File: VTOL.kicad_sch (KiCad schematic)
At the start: 36 parts, among them J10 I2C header, J5 USB_C_Receptacle_USB2.0_16P, J6 Conn_01x02_Pin, J7 Pi UART, J8 SEN66, J9 I2C header, SW1 RESET, SW2 BOOT, SW3 SW_SPDT, U4 ESP32-S3-WROOM-1, U5 USBLC6-2SC6, U6 AP7361C-33ER-13, U7 R-78E5.0-1.0

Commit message: new schem
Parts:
- removed C11: 10u 25V, Capacitor_SMD:C_0805_2012Metric_Pad1.18x1.45mm_HandSolder, symbol Device:C
- removed C13: 47u 35V, Capacitor_SMD:CP_Elec_6.3x5.8, symbol Device:C_Polarized
- removed D1: SMF5.0A, Diode_SMD:D_SOD-123F, symbol Diode:PTVS5V0Z1USK
- removed F1: 1A, Fuse:Fuse_1206_3216Metric_Pad1.42x1.75mm_HandSolder, symbol Device:Polyfuse
- removed F2: 0.75A 24V, Fuse:Fuse_1812_4532Metric_Pad1.30x3.40mm_HandSolder, symbol Device:Polyfuse
- removed H5: MountingHole, MountingHole:MountingHole_3.2mm_M3_Pad_Via, symbol Mechanical:MountingHole
- removed J10, J9: I2C header, Connector_PinHeader_2.54mm:PinHeader_1x04_P2.54mm_Vertical, symbol Connector:Conn_01x04_Pin
- removed J5: USB_C_Receptacle_USB2.0_16P, VTOL_parts:USB_C_Receptacle_GCT_USB4105-GF-A_16P_TopMnt_Horizontal_S1, symbol Connector:USB_C_Receptacle_USB2.0_16P
- removed J6: Conn_01x02_Pin, Connector_JST:JST_PH_S2B-PH-K_1x02_P2.00mm_Horizontal, symbol Connector:Conn_01x02_Pin
- removed J7: Pi UART, Connector_PinHeader_2.54mm:PinHeader_1x03_P2.54mm_Vertical, symbol Connector:Conn_01x03_Pin
- removed SW1: RESET, Button_Switch_SMD:SW_SPST_PTS645Sx43SMTR92, symbol Switch:SW_Push
- removed SW2: BOOT, Button_Switch_SMD:SW_SPST_PTS645Sx43SMTR92, symbol Switch:SW_Push
- removed SW3: SW_SPDT, VTOL_parts:SW_Slide_SPDT_RightAngle_CK_1101M2S3AQE2, symbol Switch:SW_SPDT
- removed U4: ESP32-S3-WROOM-1, VTOL_parts:ESP32-S3-WROOM-1_Via0.3mm, symbol RF_Module:ESP32-S3-WROOM-1
- removed U5: USBLC6-2SC6, Package_TO_SOT_SMD:SOT-23-6, symbol Power_Protection:USBLC6-2SC6
- removed U6: AP7361C-33ER-13, Package_TO_SOT_SMD:SOT-223-3_TabPin2, symbol Regulator_Linear:AMS1117-3.3
- removed U7: R-78E5.0-1.0, Converter_DCDC:Converter_DCDC_RECOM_R-78E-0.5_THT, symbol Converter_DCDC:R-78E5.0-1.0
- added C13: 10u 25V, Capacitor_SMD:C_0805_2012Metric_Pad1.18x1.45mm_HandSolder, symbol Device:C
- added C2: 2.2u, Capacitor_SMD:C_1206_3216Metric_Pad1.33x1.80mm_HandSolder, symbol Device:C
- added C6, C8: 47u, Capacitor_SMD:C_1206_3216Metric_Pad1.33x1.80mm_HandSolder, symbol Device:C
- added C9: 47p, Capacitor_SMD:C_0603_1608Metric_Pad1.08x0.95mm_HandSolder, symbol Device:C
- added D1: BZT52C15, Diode_SMD:D_SOD-123, symbol Device:D_Zener
- added D2: B650C, Diode_SMD:D_SMC, symbol Device:D_Schottky
- added D4: B5819W, Diode_SMD:D_SOD-123, symbol Device:D_Schottky
- added D5, D6: green, LED_SMD:LED_0603_1608Metric_Pad1.05x0.95mm_HandSolder, symbol Device:LED
- added F1: 5A slow, Fuse:Fuse_Littelfuse-NANO2-451_453, symbol Device:Fuse
- added H4: M3, MountingHole:MountingHole_3.2mm_M3, symbol Mechanical:MountingHole
- added J1: XT30PW-M, Connector_AMASS:AMASS_XT30PW-M_1x02_P2.50mm_Horizontal, symbol Connector:Conn_01x02_Pin
- added J2: USB4125-GF-A, Connector_USB:USB_C_Receptacle_GCT_USB4125-xx-x_6P_TopMnt_Horizontal, symbol Connector:USB_C_Receptacle_PowerOnly_6P
- added J3: 5V_AUX, Connector_PinHeader_2.54mm:PinHeader_1x02_P2.54mm_Vertical, symbol Connector:Conn_01x02_Pin
- added J4: FAN, Connector_PinHeader_2.54mm:PinHeader_1x02_P2.54mm_Vertical, symbol Connector:Conn_01x02_Pin
- added J5: SEN66, Connector_JST:JST_GH_BM06B-GHS-TBT_1x06-1MP_P1.25mm_Vertical, symbol Connector:Conn_01x06_Pin
- added J6, J7: I2C, Connector_PinHeader_2.54mm:PinHeader_1x04_P2.54mm_Vertical, symbol Connector:Conn_01x04_Pin
- added J9: TELEM2, Connector_JST:JST_GH_BM06B-GHS-TBT_1x06-1MP_P1.25mm_Vertical, symbol Connector:Conn_01x06_Pin
- added L1: 7.2u, Inductor_SMD:L_Coilcraft_XAL7070-XXX, symbol Device:L
- added Q1: SUD50P04-08, Package_TO_SOT_SMD:TO-252-2, symbol Transistor_FET:SUD50P04-08
- added Q2: AO3400A, Package_TO_SOT_SMD:SOT-23, symbol Transistor_FET:AO3400A
- added R10: 1k, Resistor_SMD:R_0603_1608Metric_Pad0.98x0.95mm_HandSolder, symbol Device:R
- added R11: 100, Resistor_SMD:R_0603_1608Metric_Pad0.98x0.95mm_HandSolder, symbol Device:R
- added R12: 100k, Resistor_SMD:R_0603_1608Metric_Pad0.98x0.95mm_HandSolder, symbol Device:R
- added R13, R7, R8: 10k, Resistor_SMD:R_0603_1608Metric_Pad0.98x0.95mm_HandSolder, symbol Device:R
- added R6: 16.9k, Resistor_SMD:R_0603_1608Metric_Pad0.98x0.95mm_HandSolder, symbol Device:R
- added U1: TPS54560BDDAR, Package_SO:Texas_R-PDSO-G8_EP2.95x4.9mm_Mask2.4x3.1mm_ThermalVias, symbol Regulator_Switching:TPS54560BDDA
- added U2: AP7361C-33ER-13, Package_TO_SOT_SMD:SOT-223-3_TabPin2, symbol Regulator_Linear:AMS1117-3.3
- C1: value 10u 25V -> 2.2u; footprint Capacitor_SMD:C_0805_2012Metric_Pad1.18x1.45mm_HandSolder -> Capacitor_SMD:C_1206_3216Metric_Pad1.33x1.80mm_HandSolder
- C10: value 0.1u 50V -> 4.7n
- C12: MPN (none) -> Samsung CL21A106KAQNNNE
- C14: MPN (none) -> Murata GRM31CR61A476KE15L
- C3: value 1u 50V -> 2.2u; footprint Capacitor_SMD:C_0603_1608Metric_Pad1.08x0.95mm_HandSolder -> Capacitor_SMD:C_1206_3216Metric_Pad1.33x1.80mm_HandSolder
- C4: value 0.1u 50V -> 2.2u; footprint Capacitor_SMD:C_0603_1608Metric_Pad1.08x0.95mm_HandSolder -> Capacitor_SMD:C_1206_3216Metric_Pad1.33x1.80mm_HandSolder
- C5: value 10u 25V -> 0.1u; footprint Capacitor_SMD:C_0805_2012Metric_Pad1.18x1.45mm_HandSolder -> Capacitor_SMD:C_0603_1608Metric_Pad1.08x0.95mm_HandSolder
- C7: value 10u 50V -> 47u
- H1, H2, H3: value MountingHole -> M3; footprint MountingHole:MountingHole_3.2mm_M3_Pad_Via -> MountingHole:MountingHole_3.2mm_M3; now in the parts list
- J8: value SEN66 -> PI; footprint Connector_JST:JST_GH_BM06B-GHS-TBT_1x06-1MP_P1.25mm_Vertical -> Connector_PinHeader_2.54mm:PinHeader_1x06_P2.54mm_Vertical; MPN (none) -> 2.54 mm header
- R1: value 10k -> 442k
- R2: value 10k -> 243k
- R3: value 4.7k -> 90.9k
- R4: value 4.7k -> 53.6k
- R5: value 5.1k -> 10.2k
- R9: value 5.1k -> 1k; MPN (none) -> Yageo RC0603FR-071KL
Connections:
- net 5V_FUSED is gone; now on net +BATT: C1.1
- net BATT_5V is gone; now on net +5V: C12.1
- net BOOT is gone; now on net GND: R2.2
- net CC2 is gone; now on net +5V: R9.1
- net VBUS is gone; now on net GND: C4.2
- net +3.3V: now also C13.1, J5.1 (Pin_1), J5.6 (Pin_6), J6.2 (Pin_2), J7.2 (Pin_2), R10.1, U2.2 (VO); no longer C10.1, C5.1, J8.1 (Pin_1), J8.6 (Pin_6), R1.1, R2.1, R3.1, R4.1
- net +5V: now also C7.1, R4.1, C6.1, C8.1, D4.1 (K), J2.A9 (VBUS), J2.B9 (VBUS), J3.1 (Pin_1), J4.1 (Pin_1), L1.2, R7.2, R8.2, U2.3 (VI)
- net +BATT: now also C3.1, C4.1, R1.2, C2.1, D1.1 (K), Q1.3 (S), U1.2 (VIN); no longer C7.1
- net GND: now also C3.2, J8.1 (Pin_1), R3.2, C13.2, C2.2, C6.2, C8.2, C9.2, D2.2 (A), D5.1 (K), D6.1 (K), J1.1 (Pin_1), J2.A12 (GND), J2.B12 (GND), J2.SH (SHIELD), J3.2 (Pin_2), J5.2 (Pin_2), J5.5 (Pin_5), J6.1 (Pin_1), J7.1 (Pin_1), J9.6 (Pin_6), Q2.2 (S), R12.2, R13.2, U1.7 (GND), U1.9 (GND), U2.1 (GND); no longer C3.1, C4.1, C5.2, J8.2 (Pin_2), J8.5 (Pin_5), R9.2
- net SCL: now also J8.3 (Pin_3), J5.4 (Pin_4), J6.4 (Pin_4), J7.4 (Pin_4); no longer J8.4 (Pin_4), R4.2
- net SDA: now also J8.2 (Pin_2), J5.3 (Pin_3), J6.3 (Pin_3), J7.3 (Pin_3); no longer J8.3 (Pin_3), R3.2
- net CC1 renamed FB
- net FB: now also R4.2, U1.5 (FB)
- removed net EN: C3.2, R1.2
- new net: C5.2, U1.1 (BOOT)
- new net: R1.1, R3.1, U1.3 (EN)
- new net: R2.1, U1.4 (RT/CLK)
- new net: C5.1, D2.1 (K), L1.1, U1.8 (SW)
- new net: C10.1, R6.2
- new net: D1.2 (A), Q1.1 (G), R13.1
- new net: Q2.1 (G), R11.2, R12.1
- new net: D5.2 (A), R9.2
- new net: J2.A5 (CC1), R7.1
- new net: J2.B5 (CC2), R8.1
- new net: D6.2 (A), R10.2
- new net COMP: C9.1, R6.1, U1.6 (COMP)
- new net FAN_CTRL: J8.6 (Pin_6), R11.1
- new net FAN_SW: D4.2 (A), J4.2 (Pin_2), Q2.3 (D)
- new net PI_RX: J8.5 (Pin_5), J9.2 (Pin_2)
- new net PI_TX: J8.4 (Pin_4), J9.3 (Pin_3)
- new net VBAT_F: F1.2, Q1.2 (D)
- new net VBAT_IN: F1.1, J1.2 (Pin_2)
- no-connect marks 31 -> 3
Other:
- note added: "1 Cube +5V (not used) 2 Cube TX -> Pi RX 3 Cube RX <- Pi TX 4 CTS, 5 RTS (not used) 6 GND ArduPilot: SERIAL2_PROTOCOL=2, SERIAL2_BAUD=921"
- note added: "1 GND -> Pi pin 6 2 SDA -> Pi pin 3 (GPIO2) 3 SCL -> Pi pin 5 (GPIO3) 4 PI_TX <- Pi pin 8 (GPIO14 TXD) 5 PI_RX -> Pi pin 10 (GPIO15 RXD) 6 FAN_CTRL <- Pi pin 12 (GPIO18)"
- note added: "3.3 V SENSOR RAIL + I2C"
- note added: "5 V / 5 A BUCK (TPS54560B, 400 kHz, UVLO on 10.9 V / off 9.7 V)"
- note added: "5 V OUTPUTS (Pi 4 over USB-C, spare 5 V, fan)"
- note added: "BATTERY INPUT (4S LiPo, 12.8 - 16.8 V)"
- note added: "CC pull-ups 10k to 5 V = source advertising 3 A"
- note added: "CUBE TELEM2 (JST GH 6-pin, straight cable)"
- note added: "Fan off unless the Pi drives FAN_CTRL high (dtoverlay=gpio-fan)"
- note added: "I2C expansion (GND / 3V3 / SDA / SCL)"
- note added: "PI 4 LINK (Dupont to Pi GPIO)"
- note added: "SEN66 (JST GH 6-pin)"
- note removed: "Air quality + temp/RH (SEN66, J8) I2C expansion headers (J9, J10)"
- note removed: "Battery Input"
- note removed: "CONTROL MODULE"
- note removed: "I2C BUS PULL-UPS"
- note removed: "RASPBERRY PI UART LINK (J7) Camera plugs into the Pi directly"
- note removed: "SENSOR CONNECTORS"
- title: Module Control Board -> Pi Power and Sensor Board

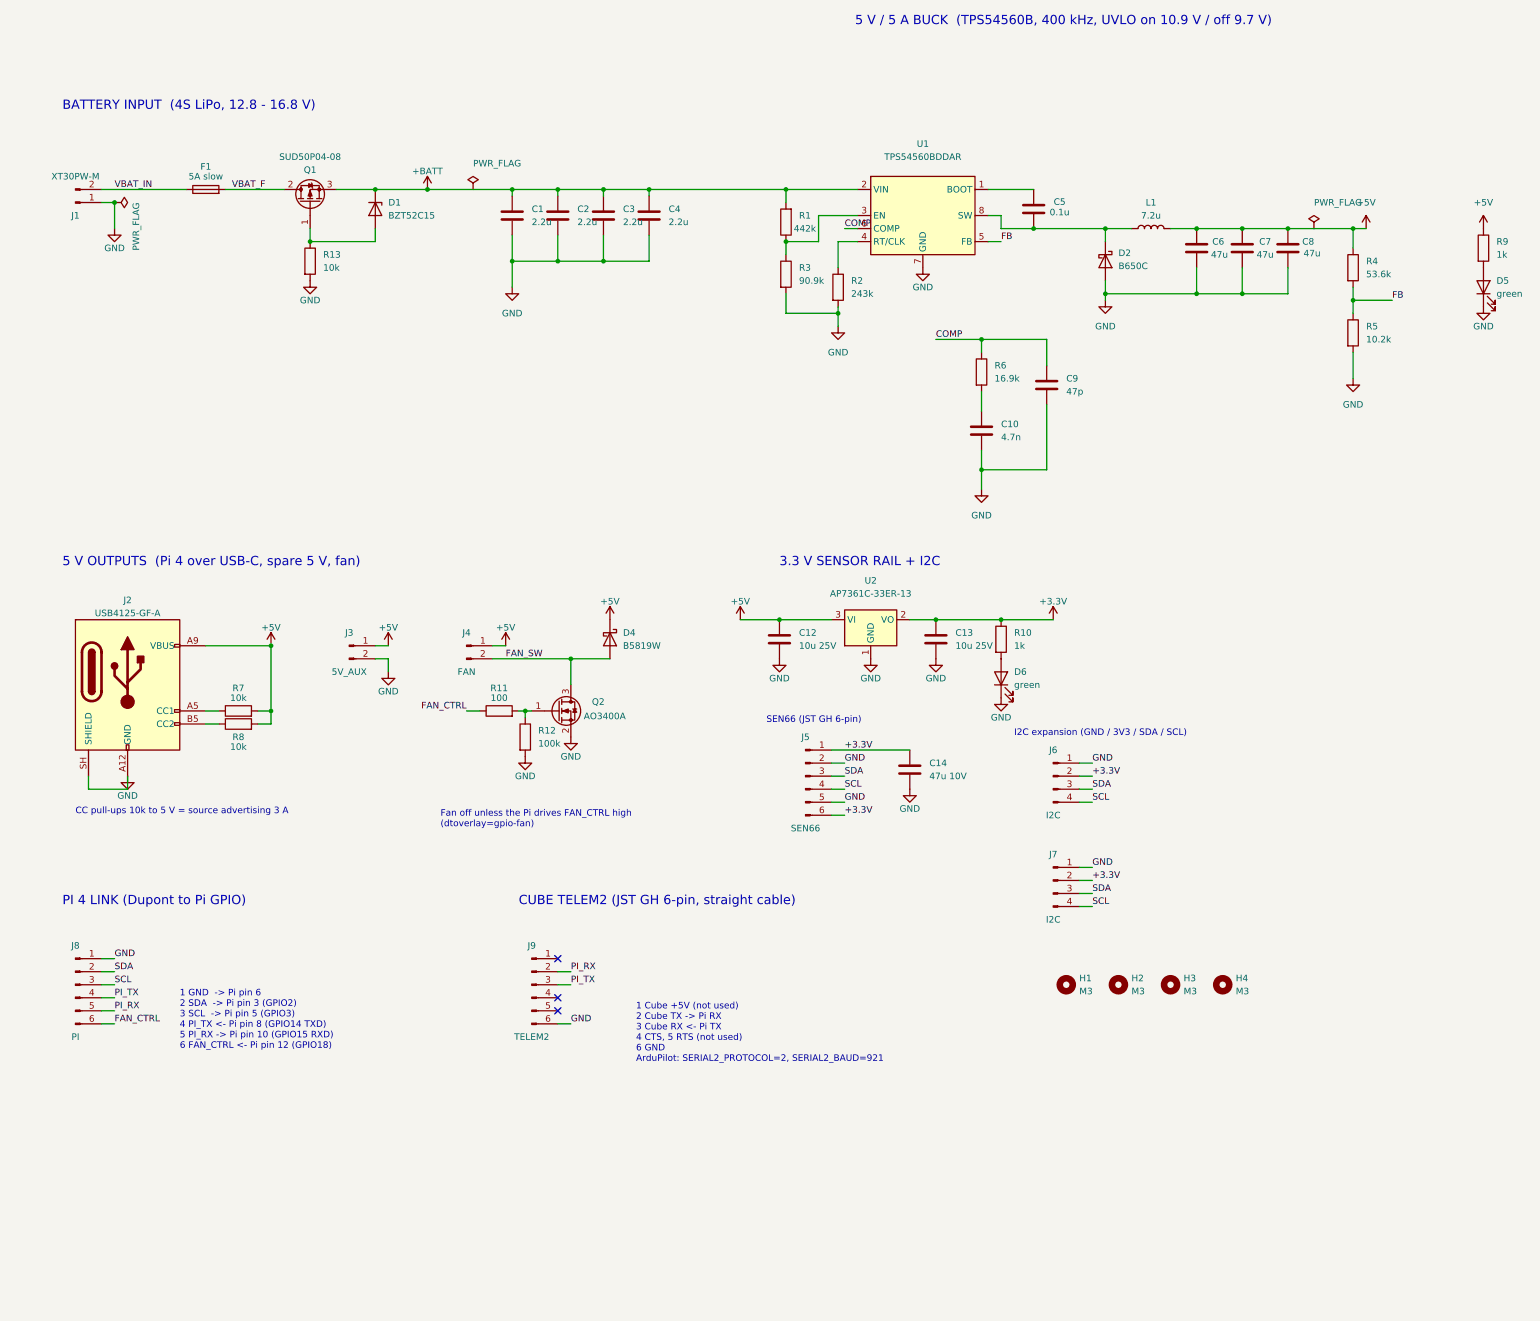
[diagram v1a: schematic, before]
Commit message: Add INA226 power monitor, finish part selection, clear PCB
- Schematic: INA226 (U1) + 20m shunt (R3) + C2 on the 5V rail, I2C 0x44
- Sections boxed and titled; on-sheet notes removed
- Footprint and DigiKey part # set for every part
- J8 -> Molex 0702461201 with 1.1mm-drill IDC 2x06 footprint
- D6 -> red LED on 3.3V
- PCB cleared for re-layout
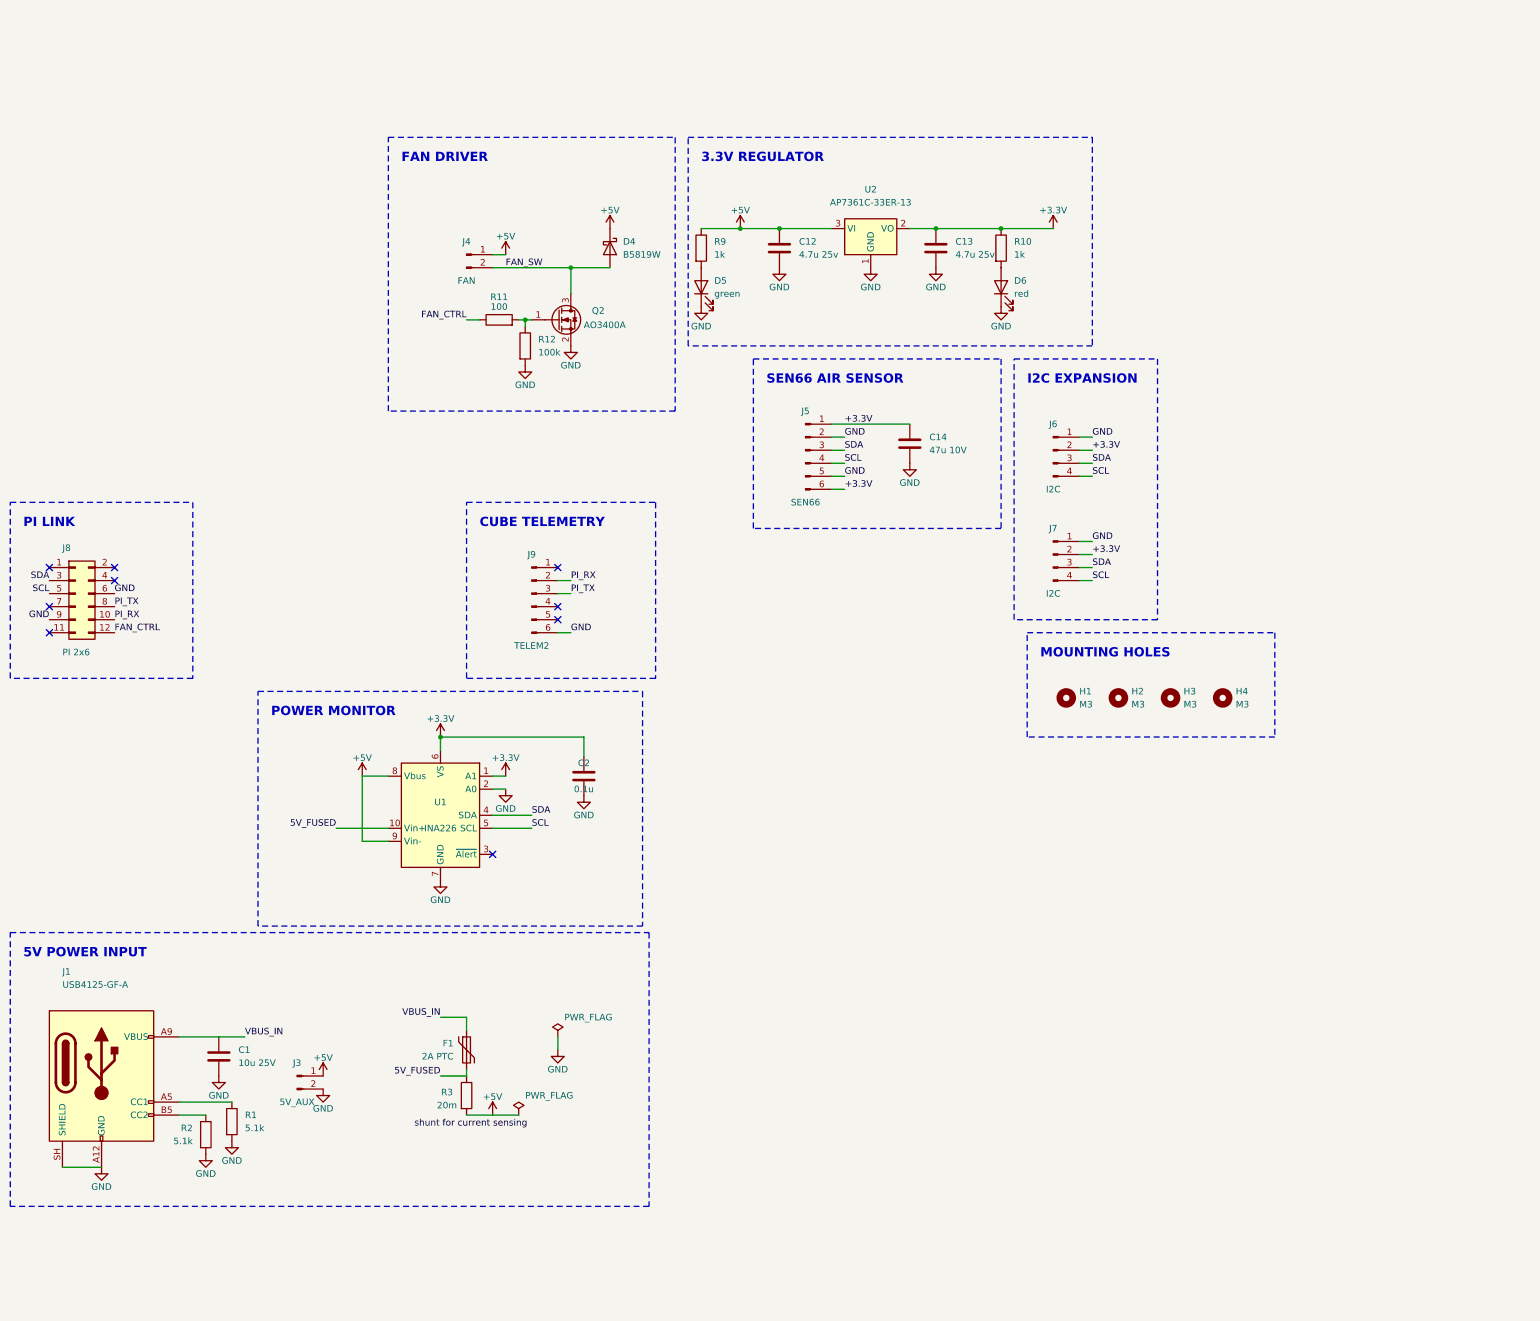
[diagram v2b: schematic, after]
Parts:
- removed C10: 4.7n, Capacitor_SMD:C_0603_1608Metric_Pad1.08x0.95mm_HandSolder, symbol Device:C
- removed C3, C4: 2.2u, Capacitor_SMD:C_1206_3216Metric_Pad1.33x1.80mm_HandSolder, symbol Device:C
- removed C5: 0.1u, Capacitor_SMD:C_0603_1608Metric_Pad1.08x0.95mm_HandSolder, symbol Device:C
- removed C6, C7, C8: 47u, Capacitor_SMD:C_1206_3216Metric_Pad1.33x1.80mm_HandSolder, symbol Device:C
- removed C9: 47p, Capacitor_SMD:C_0603_1608Metric_Pad1.08x0.95mm_HandSolder, symbol Device:C
- removed D1: BZT52C15, Diode_SMD:D_SOD-123, symbol Device:D_Zener
- removed D2: B650C, Diode_SMD:D_SMC, symbol Device:D_Schottky
- removed F1: 5A slow, Fuse:Fuse_Littelfuse-NANO2-451_453, symbol Device:Fuse
- removed J1: XT30PW-M, Connector_AMASS:AMASS_XT30PW-M_1x02_P2.50mm_Horizontal, symbol Connector:Conn_01x02_Pin
- removed J2: USB4125-GF-A, Connector_USB:USB_C_Receptacle_GCT_USB4125-xx-x_6P_TopMnt_Horizontal, symbol Connector:USB_C_Receptacle_PowerOnly_6P
- removed J8: PI, Connector_PinHeader_2.54mm:PinHeader_1x06_P2.54mm_Vertical, symbol Connector:Conn_01x06_Pin
- removed L1: 7.2u, Inductor_SMD:L_Coilcraft_XAL7070-XXX, symbol Device:L
- removed Q1: SUD50P04-08, Package_TO_SOT_SMD:TO-252-2, symbol Transistor_FET:SUD50P04-08
- removed R13, R7, R8: 10k, Resistor_SMD:R_0603_1608Metric_Pad0.98x0.95mm_HandSolder, symbol Device:R
- removed R4: 53.6k, Resistor_SMD:R_0603_1608Metric_Pad0.98x0.95mm_HandSolder, symbol Device:R
- removed R5: 10.2k, Resistor_SMD:R_0603_1608Metric_Pad0.98x0.95mm_HandSolder, symbol Device:R
- removed R6: 16.9k, Resistor_SMD:R_0603_1608Metric_Pad0.98x0.95mm_HandSolder, symbol Device:R
- removed U1: TPS54560BDDAR, Package_SO:Texas_R-PDSO-G8_EP2.95x4.9mm_Mask2.4x3.1mm_ThermalVias, symbol Regulator_Switching:TPS54560BDDA
- added F1: 2A PTC, Fuse:Fuse_1812_4532Metric, symbol Device:Polyfuse
- added J1: USB4125-GF-A, Connector_USB:USB_C_Receptacle_GCT_USB4125-xx-x_6P_TopMnt_Horizontal, symbol Connector:USB_C_Receptacle_PowerOnly_6P
- added J8: PI 2x6, VTOL_parts:IDC-Header_2x06_P2.54mm_Vertical_Drill1.1, symbol Connector_Generic:Conn_02x06_Odd_Even
- added U1: INA226, Package_SO:MSOP-10_3x3mm_P0.5mm, symbol Sensor_Energy:INA226
- C1: value 2.2u -> 10u 25V; footprint Capacitor_SMD:C_1206_3216Metric_Pad1.33x1.80mm_HandSolder -> Capacitor_SMD:C_0805_2012Metric_Pad1.18x1.45mm_HandSolder; Digikey Part # (none) -> 4713-GMC21X7R106K25NTCT-ND; MPN (none) -> Cal-Chip GMC21X7R106K25NT
- C12, C13: value 10u 25V -> 4.7u 25v; Digikey Part # (none) -> 587-2990-1-ND; MPN Samsung CL21A106KAQNNNE -> Taiyo Yuden TMK212AB7475KG-T
- C14: Digikey Part # (none) -> 399-C1206C476M8PACTUCT-ND; MPN Murata GRM31CR61A476KE15L -> KEMET C1206C476M8PACTU
- C2: value 2.2u -> 0.1u; footprint Capacitor_SMD:C_1206_3216Metric_Pad1.33x1.80mm_HandSolder -> Capacitor_SMD:C_0603_1608Metric_Pad1.08x0.95mm_HandSolder; Digikey Part # (none) -> 399-C0603C104K3RACTUCT-ND; MPN (none) -> KEMET C0603C104K3RACTU
- D4: Digikey Part # (none) -> 5399-B5819WCT-ND
- D5: Digikey Part # (none) -> 732-4971-1-ND
- D6: value green -> red; Digikey Part # (none) -> 732-4978-1-ND; MPN Wurth 150060GS75000 -> Wurth 150060RS75000
- J3, J4: Digikey Part # (none) -> 35-PRPC002SAAN-RC-ND; MPN 2.54 mm header -> Sullins PRPC002SAAN-RC
- J5, J9: Digikey Part # (none) -> 455-BM06B-GHS-TBTCT-ND
- J6, J7: Digikey Part # (none) -> 35-PRPC004SAAN-RC-ND; MPN 2.54 mm header -> Sullins PRPC004SAAN-RC
- Q2: Digikey Part # (none) -> 785-1000-1-ND
- R1: value 442k -> 5.1k; Digikey Part # (none) -> P5.10KHCT-ND; MPN (none) -> Panasonic ERJ-3EKF5101V
- R10, R9: Digikey Part # (none) -> P1.00KHCT-ND; MPN Yageo RC0603FR-071KL -> Panasonic ERJ-3EKF1001V
- R11: Digikey Part # (none) -> P100HCT-ND; MPN Yageo RC0603FR-07100RL -> Panasonic ERJ-3EKF1000V
- R12: Digikey Part # (none) -> CR0603-FX-1003ELFCT-ND; MPN Yageo RC0603FR-07100KL -> Bourns CR0603-FX-1003ELF
- R2: value 243k -> 5.1k; Digikey Part # (none) -> P5.10KHCT-ND; MPN (none) -> Panasonic ERJ-3EKF5101V
- R3: value 90.9k -> 20m; footprint Resistor_SMD:R_0603_1608Metric_Pad0.98x0.95mm_HandSolder -> Resistor_SMD:R_1206_3216Metric_Pad1.30x1.75mm_HandSolder; Digikey Part # (none) -> CSR1206FK20L0CT-ND; MPN (none) -> Stackpole CSR1206FK20L0
- U2: Digikey Part # (none) -> AP7361C-33ER-13DICT-ND
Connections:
- net +3.3V: now also C2.1, U1.1 (A1), U1.6 (VS)
- net +5V: now also R3.2, U1.8 (Vbus), U1.9 (Vin-)
- net FAN_CTRL: now also J8.12 (Pin_12)
- net GND: now also R1.2, J1.A12 (GND), J1.B12 (GND), J1.SH (SHIELD), J8.6 (Pin_6), J8.9 (Pin_9), U1.2 (A0), U1.7 (GND); no longer R3.2
- net PI_RX: now also J8.10 (Pin_10)
- net PI_TX: now also J8.8 (Pin_8)
- net SCL: now also J8.5 (Pin_5), U1.5 (SCL)
- net SDA: now also J8.3 (Pin_3), U1.4 (SDA)
- net at R1.1: now also J1.A5 (CC1); no longer R3.1
- net at R2.1: now also J1.B5 (CC2)
- removed net +BATT: C1.1, C2.1, R1.2
- new net 5V_FUSED: F1.2, R3.1, U1.10 (Vin+)
- new net VBUS_IN: C1.1, F1.1, J1.A9 (VBUS), J1.B9 (VBUS)
- no-connect marks 3 -> 9
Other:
- note added: "3.3V REGULATOR"
- note added: "5V POWER INPUT"
- note added: "CUBE TELEMETRY"
- note added: "FAN DRIVER"
- note added: "I2C EXPANSION"
- note added: "MOUNTING HOLES"
- note added: "PI LINK"
- note added: "POWER MONITOR"
- note added: "SEN66 AIR SENSOR"
- note removed: "1 Cube +5V (not used) 2 Cube TX -> Pi RX 3 Cube RX <- Pi TX 4 CTS, 5 RTS (not used) 6 GND ArduPilot: SERIAL2_PROTOCOL=2, SERIAL2_BAUD=921"
- note removed: "1 GND -> Pi pin 6 2 SDA -> Pi pin 3 (GPIO2) 3 SCL -> Pi pin 5 (GPIO3) 4 PI_TX <- Pi pin 8 (GPIO14 TXD) 5 PI_RX -> Pi pin 10 (GPIO15 RXD) 6 FAN_CTRL <- Pi pin 12 (GPIO18)"
- note removed: "3.3 V SENSOR RAIL + I2C"
- note removed: "5 V / 5 A BUCK (TPS54560B, 400 kHz, UVLO on 10.9 V / off 9.7 V)"
- note removed: "5 V OUTPUTS (Pi 4 over USB-C, spare 5 V, fan)"
- note removed: "BATTERY INPUT (4S LiPo, 12.8 - 16.8 V)"
- note removed: "CC pull-ups 10k to 5 V = source advertising 3 A"
- note removed: "CUBE TELEM2 (JST GH 6-pin, straight cable)"
- note removed: "Fan off unless the Pi drives FAN_CTRL high (dtoverlay=gpio-fan)"
- note removed: "I2C expansion (GND / 3V3 / SDA / SCL)"
- note removed: "PI 4 LINK (Dupont to Pi GPIO)"
- note removed: "SEN66 (JST GH 6-pin)"
- moved on the sheet: C12, C13, C14, D4, D5, D6, H1, H2, H3, H4, J4, J5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
